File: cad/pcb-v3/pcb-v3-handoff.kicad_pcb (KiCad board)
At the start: 4 copper layers, 19.3 x 19.3 mm, 46 parts

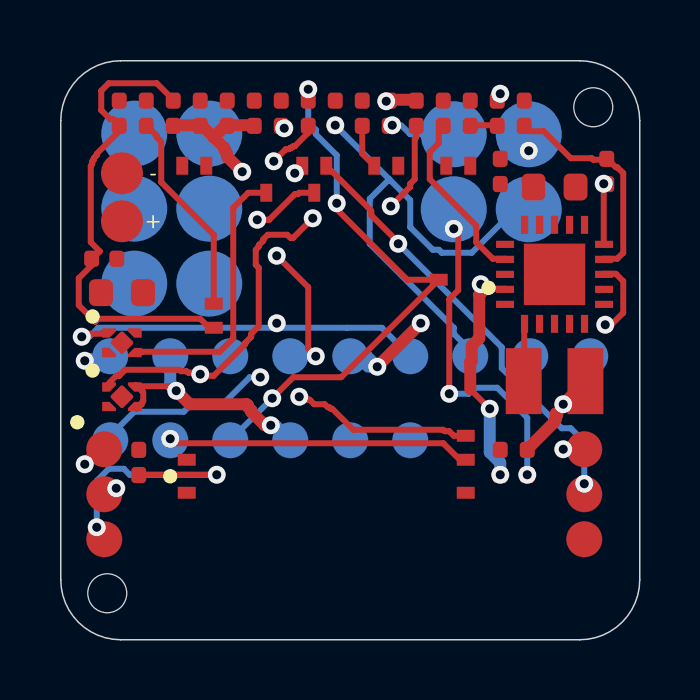
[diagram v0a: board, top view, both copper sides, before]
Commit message: C7 out of the right column so U2 gets a via lane: opens 7->5, boxed-in pads 3->1. 12/15 preflight checks pass.
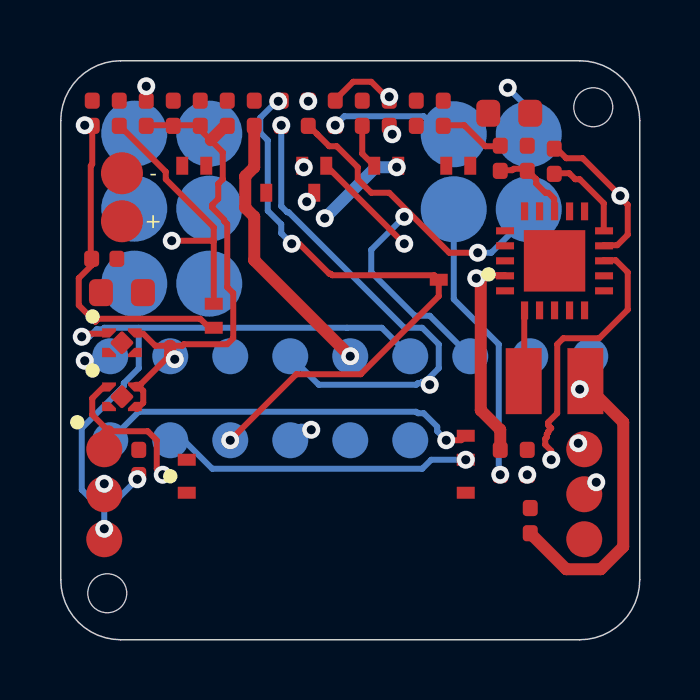
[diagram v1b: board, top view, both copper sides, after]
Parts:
- moved ROK1 11.6 mm to (5.90, 3.74)
- moved C7 2.89 mm to (5.30, -7.90)
- moved ROV1 2.72 mm to (3.10, -7.90)
- moved C1 2.18 mm to (6.00, 5.68)
- moved ROK3 1.80 mm to (5.90, -6.40)
- moved ROV2 1.80 mm to (5.00, -6.40)
- moved R1 1.80 mm to (-0.50, -7.90)
- moved ROK2 1.78 mm to (6.80, -6.30)
- moved C10 0.90 mm to (-5.90, -7.90)
- moved C13 0.90 mm to (-7.70, -7.90)
- moved C3 0.90 mm to (-5.00, -7.90)
- moved C6 0.90 mm to (-3.20, -7.90)
- moved R3 0.90 mm to (5.00, 3.74)
- moved R2 0.90 mm to (1.30, -7.90)
- moved C4 0.90 mm to (2.20, -7.90)
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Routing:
- net VSTOR: track 21.1 -> 36.2 mm, vias 3 -> 4
- net OK_PROG: track 7.43 -> 18.4 mm, vias 0 -> 2
- net VIN_DC: track 38.9 -> 49.2 mm, vias 6 -> 4
- net SENSOR_SW_EN: track 8.99 -> 0.00 mm
- net BL_FLAG: track 6.90 -> 15.6 mm, vias 0 -> 2
- net SENSOR_3V3: track 30.9 -> 22.7 mm, vias 6 -> 2
- net HARV_2: track 14.3 -> 6.53 mm
- net VREF_SAMP: track 5.83 -> 0.00 mm
- net VBAT_OK: track 25.1 -> 30.9 mm, vias 4 -> 3
- net SENSOR_MCU_3V3: track 27.1 -> 22.0 mm, vias 4 -> 3
- net SENSOR_TX: track 17.5 -> 13.3 mm
- net OK_HYST: track 7.01 -> 3.01 mm, vias 2 -> 0
- net HARV_1: track 1.87 -> 4.32 mm
- net VBAT_OV_SET: track 0.00 -> 2.23 mm
- net RESET: track 18.3 -> 20.3 mm
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
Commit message: Correct the open-connection metric: zero-copper nets never appeared as 'disconnected', so the loop could delete a net and score it a win. True count is 11, not 3. The 3 dead nets route fine alone -> ordering, not geometry; seeding them first costs more than it saves.
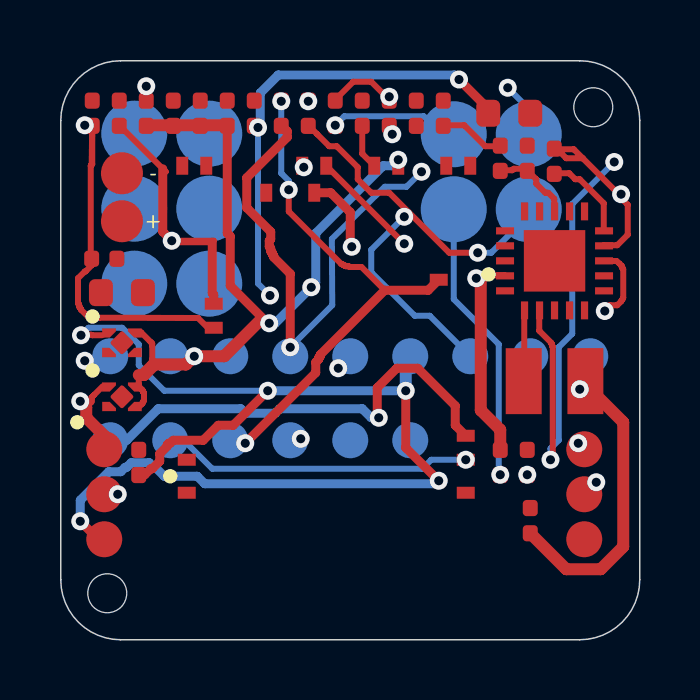
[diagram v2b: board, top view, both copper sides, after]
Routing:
- net VSTOR: track 36.2 -> 56.9 mm, vias 4 -> 7
- net SENSOR_MCU_3V3: track 22.0 -> 37.5 mm, vias 3 -> 5
- net SENSOR_3V3: track 22.7 -> 33.4 mm, vias 2 -> 5
- net SENSOR_WAKEUP: track 12.9 -> 18.5 mm
- net VBAT_OK: track 30.9 -> 28.2 mm
- net RESET: track 20.3 -> 17.8 mm
- net SWDIO: track 12.8 -> 15.1 mm
- net OK_PROG: track 18.4 -> 19.8 mm
- net VBAT_SENSE: track 14.7 -> 16.0 mm
- net BL_FLAG: track 15.6 -> 16.3 mm

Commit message: Design rule 0.20 -> 0.127: U3/U4 pads are 0.34-0.40mm apart and a 0.20 track needs 0.60 to pass. Opens 13->5, no dead nets, DRC clean. Ship a matching .kicad_pro so rules are not stale.
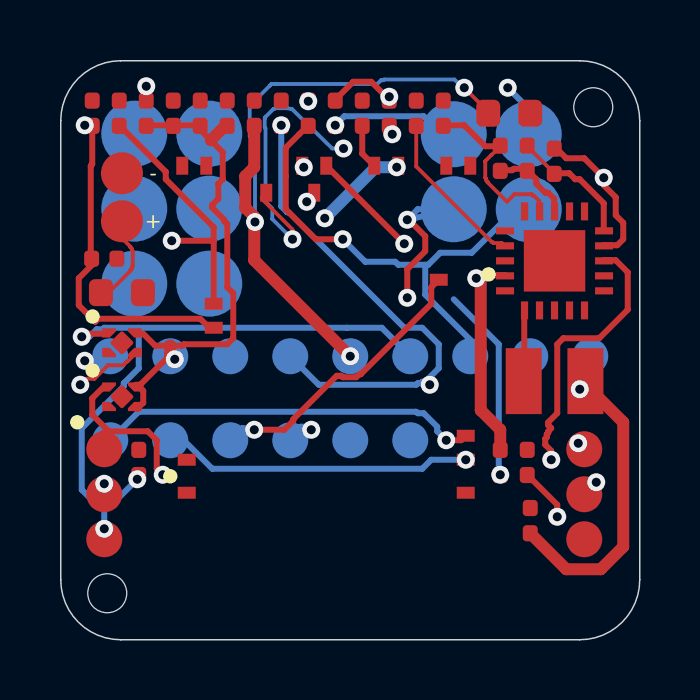
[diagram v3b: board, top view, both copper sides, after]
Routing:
- net SENSOR_SW_EN: track 0.00 -> 24.7 mm, vias 0 -> 3
- net VSTOR: track 56.9 -> 36.2 mm, vias 7 -> 4
- net SENSOR_MCU_3V3: track 37.5 -> 22.0 mm, vias 5 -> 3
- net HARV_3: track 9.42 -> 21.0 mm, vias 1 -> 3
- net RESET: track 17.8 -> 9.60 mm, vias 3 -> 1
- net SENSOR_WAKEUP: track 18.5 -> 12.9 mm
- net VREF_SAMP: track 0.00 -> 5.40 mm
- net VBAT_OV_SET: track 2.23 -> 6.18 mm
- net VBAT: track 0.00 -> 3.34 mm
- net VBAT_OK: track 28.2 -> 30.9 mm
- net SWDIO: track 15.1 -> 12.8 mm
- net SENSOR_3V3: track 33.4 -> 35.4 mm, vias 5 -> 4
- net VBAT_SENSE: track 16.0 -> 14.7 mm
- net OK_HYST: track 3.01 -> 4.30 mm
- net BL_FLAG: track 16.3 -> 15.6 mm
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
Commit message: ZERO open connections: 15/15 preflight checks pass
Four causes, not one:
 - test points placed decoratively in a row instead of by net locality
   (and polluting every net centroid, dragging the passives with them)
 - parts sitting on pogo pads, where a through-hole via would come out
   through the mating contact
 - CHAN still reserving 0.60mm channels sized for the retired 0.20 rule
 - net ORDER: OK_PROG took the one-track corridor east of U2 and ran 10mm
   up the board edge, walling VBAT_OK's pin in. Rip the squatter, re-route
   it after the pin it starved.

Also fixes four checkers that were lying: preflight used a relative board
path under cwd=KRT, check_board hard-coded 0.127, the handoff board shipped
without its .kicad_pro so rules were stale, and nudge.py matched a number
format the file does not use. Adds sexp.py, a real parser, to replace regex
pad parsing that has now caused three silent wrong answers.
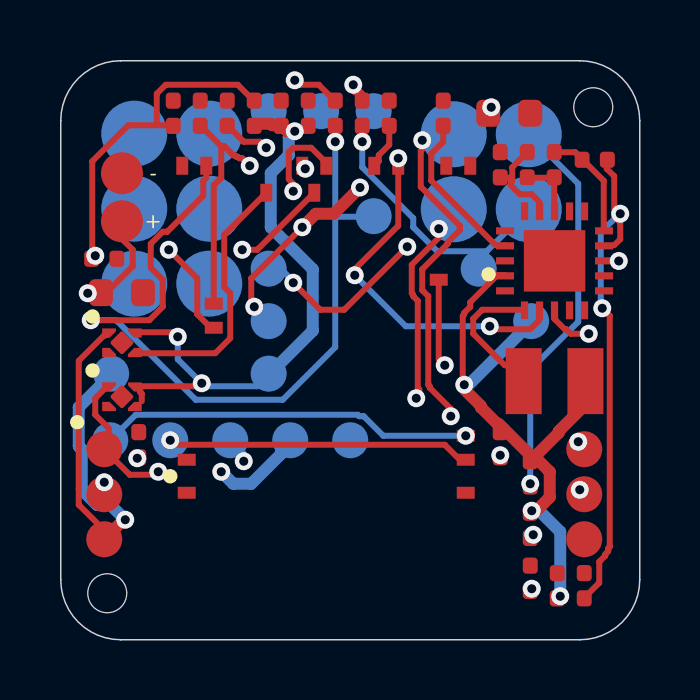
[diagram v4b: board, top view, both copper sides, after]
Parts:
- moved C10 19.5 mm to (6.00, 7.60)
- moved TP1 14.1 mm to (6.03, -0.97)
- moved R2 12.9 mm to (6.00, 4.12)
- moved R1 12.3 mm to (5.00, 3.15)
- moved TP9 12.1 mm to (-0.97, -7.97)
- moved TP8 11.9 mm to (-2.72, -7.97)
- moved TP10 11.0 mm to (0.78, -7.97)
- moved TP6 9.99 mm to (-7.97, 0.78)
- moved TP4 5.43 mm to (0.78, -4.47)
- moved ROK1 4.53 mm to (7.80, 7.85)
- moved C3 3.60 mm to (-1.40, -7.90)
- moved R4 3.60 mm to (-3.20, -7.90)
- moved TP2 3.33 mm to (-2.72, 0.78)
- moved TP3 3.19 mm to (-2.72, -2.72)
- moved TP5 2.96 mm to (-2.72, -0.97)
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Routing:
- net VIN_DC: track 49.2 -> 19.6 mm, vias 4 -> 3
- net VBAT: track 3.34 -> 27.0 mm, vias 0 -> 4
- net VSTOR: track 36.2 -> 53.5 mm, vias 4 -> 8
- net RESET: track 9.60 -> 26.3 mm, vias 1 -> 3
- net SENSOR_SW_EN: track 24.7 -> 8.95 mm, vias 3 -> 0
- net HARV_1: track 4.32 -> 14.2 mm, vias 1 -> 3
- net VBAT_OK: track 30.9 -> 39.9 mm
- net BL_RETURN: track 16.4 -> 9.13 mm
- net SENSOR_3V3: track 35.4 -> 28.4 mm, vias 4 -> 6
- net HARV_3: track 21.0 -> 14.4 mm
- net HARV_2: track 6.53 -> 13.0 mm, vias 2 -> 1
- net SENSOR_MCU_3V3: track 22.0 -> 16.9 mm, vias 3 -> 2
- net VBAT_OV_SET: track 6.18 -> 3.23 mm
- net OK_PROG: track 19.8 -> 17.1 mm
- net LX: track 2.45 -> 4.74 mm
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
